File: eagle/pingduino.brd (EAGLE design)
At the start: 98.4 x 80 mm, 35 parts, among them IC1 ATMEGA328, IC3 74LS595N, IC4 74LS595N, IC5 74LS595N, IC6 74LS595N, IC7 74HC14N, Q1 16MHz

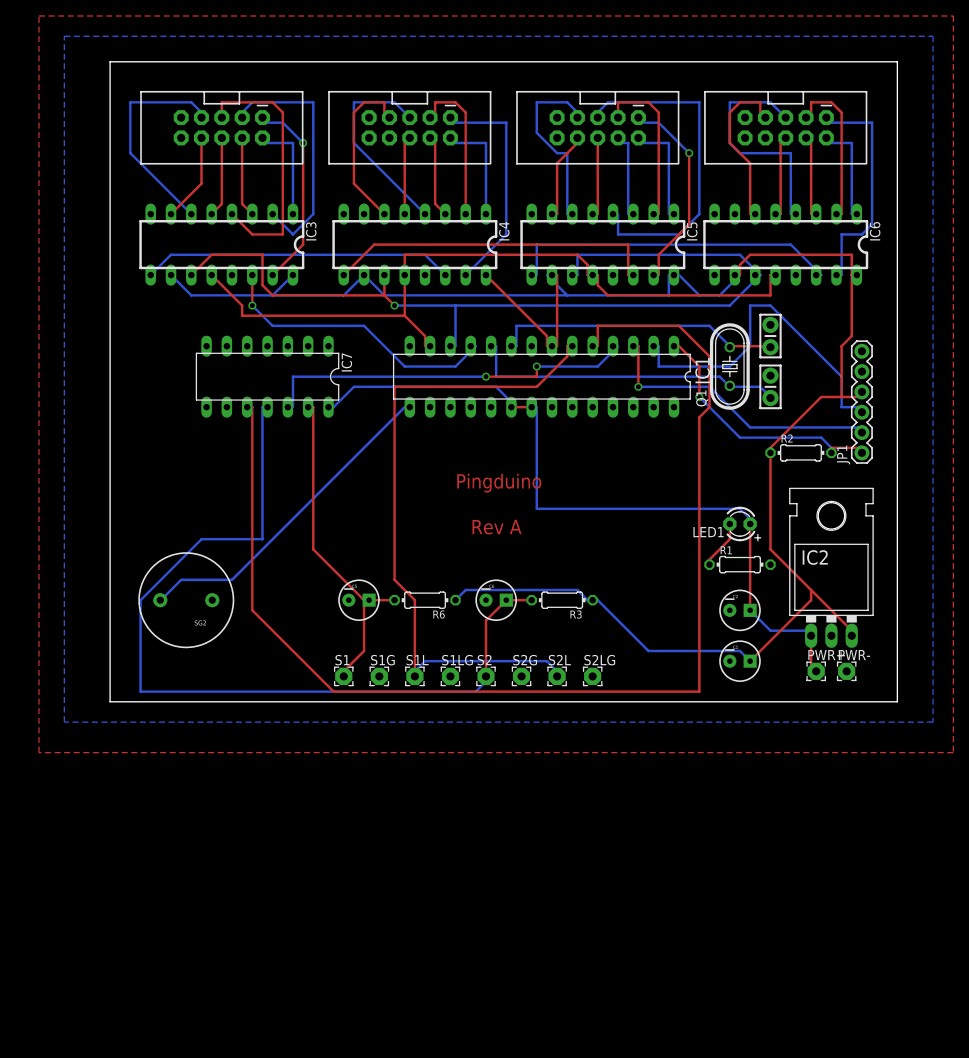
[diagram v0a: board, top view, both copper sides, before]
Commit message: Re-route the 5x2 headers so I can actually solder them.
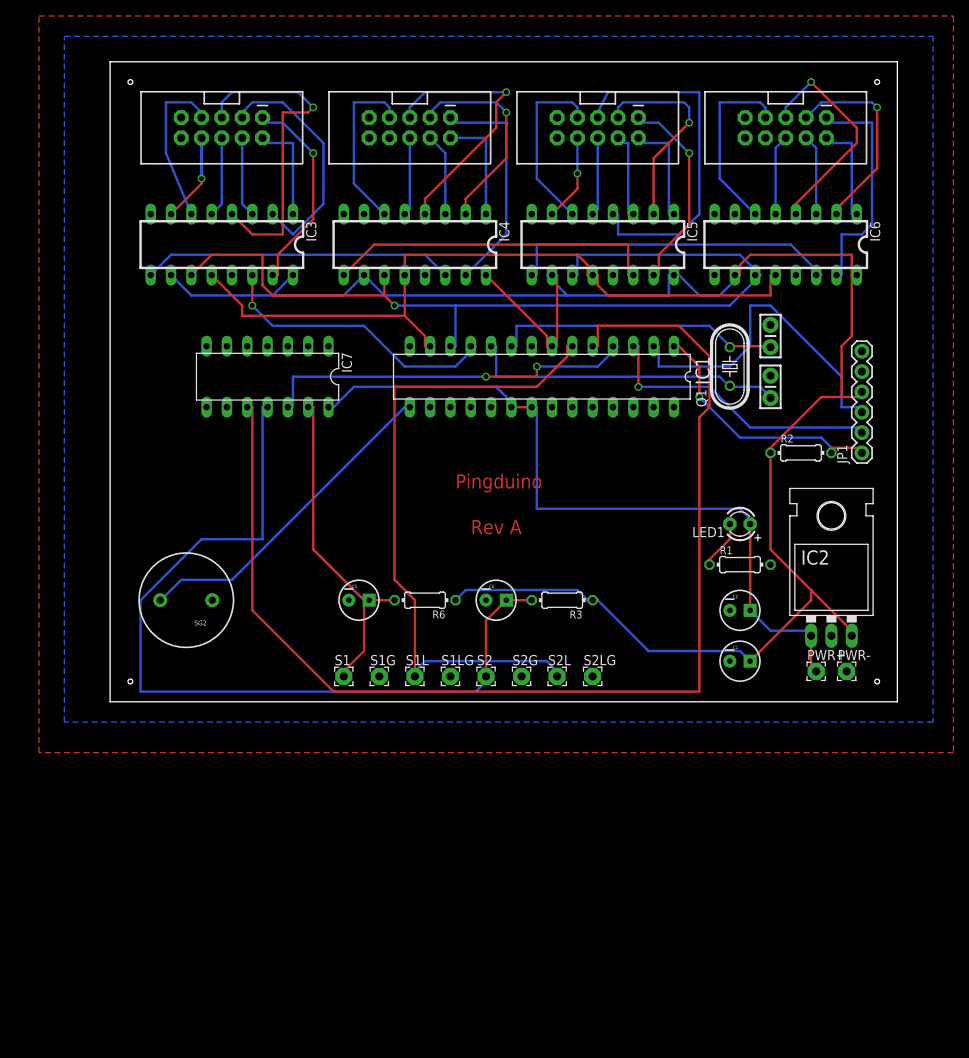
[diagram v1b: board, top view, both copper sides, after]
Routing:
- net D1E: track 32.7 -> 41.4 mm, vias 0 -> 1
- net D2E: track 25.4 -> 33.6 mm
- net D1G: track 27.2 -> 20.2 mm
- net D2C: track 19.2 -> 26.0 mm
- net D4C: track 19.8 -> 25.4 mm
- net D3C: track 20.8 -> 25.9 mm
- net D3E: track 42.2 -> 44.5 mm
- net D4G: track 20.9 -> 23.1 mm
- net D4E: track 29.3 -> 27.8 mm
- net D1A: track 24.9 -> 26.3 mm
- net D1C: track 31.2 -> 30.0 mm
- net D3G: track 23.2 -> 22.4 mm
- net D2G: track 20.8 -> 21.5 mm
- net D1P: vias 0 -> 1

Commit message: Add Garan audio module and amplifier to schematic and board
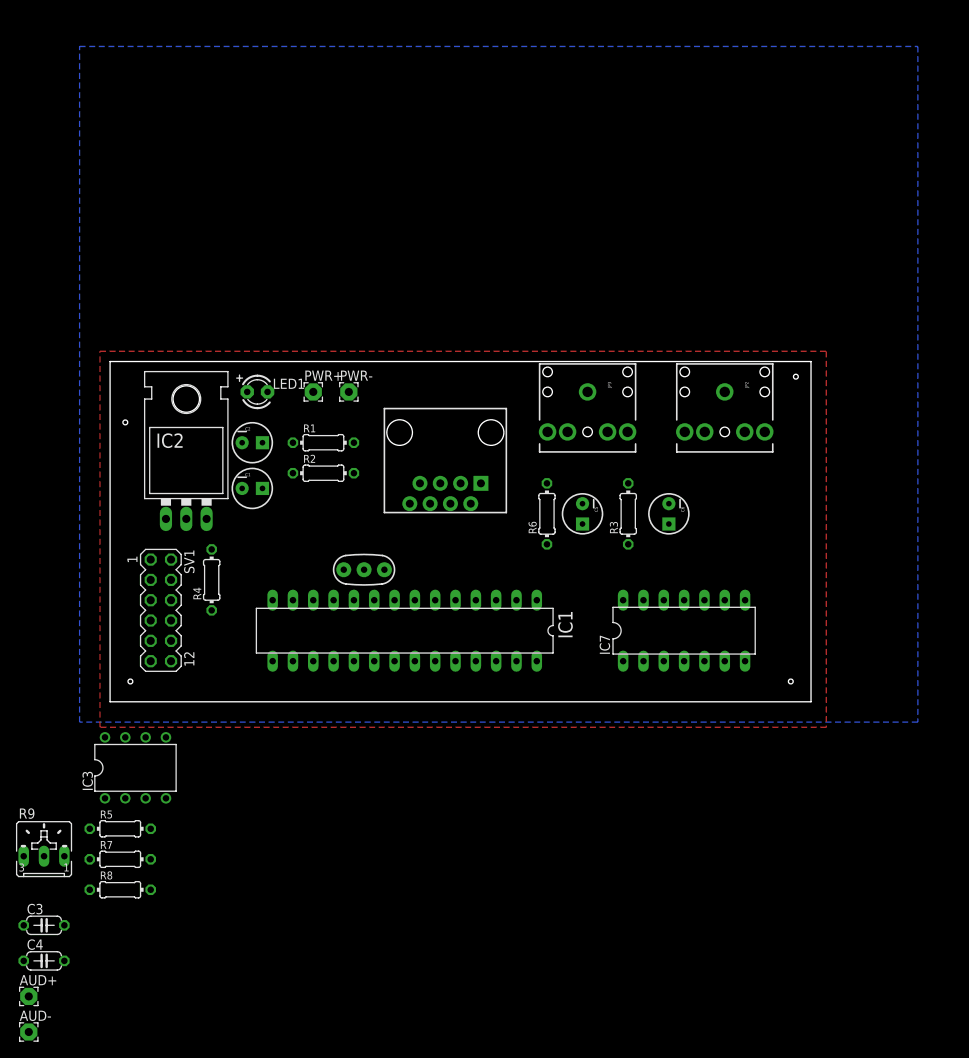
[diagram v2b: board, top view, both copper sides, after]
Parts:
- removed IC4, IC5, IC6: 74LS595N, SparkFun-DigitalIC:DIL16
- removed JP1: (no value), SparkFun-Connectors:1X06
- removed JP4, JP5: (no value), SparkFun-Connectors:2X5-SHROUDED
- removed Q1: 16MHz, adafruit:HC49U-V
- removed S1, S1G, S1L, S1LG, S2, S2G, S2L, S2LG: (no value), wirepad:2,15/1,0
- removed SG2: BUZZER, SparkFun-Electromechanical:BUZZER-12MM
- added AUD+, AUD-: (no value), wirepad:2,15/1,0
- added R4, R5, R7, R8: 1k, resistor:0204/7
- added R9: (no value), pot:B25U
- added SV1: (no value), con-lstb:MA06-2
- added U$1: RJ45-8PTH, SparkFun-Connectors:RJ45-8
- added Y1: (no value), SparkFun-FreqCtrl:RESONATOR-PTH
- C3, C4: value 22p -> (none); device SparkFun-Capacitors:CAP-PTH-SMALL-KIT -> rcl:C050-024X044
- IC3: value 74LS595N -> LM386N-3; device SparkFun-DigitalIC:DIL16 -> linear:DIL08
- JP2, JP3: device SparkFun-Connectors:2X5-SHROUDED -> SparkFun-Connectors:AUDIO-JACK
- moved C4 119.8 mm to (-8.26, -32.4), turned to 0 degrees
- moved C3 113.0 mm to (-8.26, -27.9), turned to 0 degrees
- moved IC2 82.0 mm to (9.53, 26.7)
- moved PWR+ 71.9 mm to (25.4, 38.7)
- moved PWR- 71.4 mm to (29.8, 38.7)
- moved JP2 71.0 mm to (76.8, 38.7)
- moved IC3 66.3 mm to (3.17, -8.26), turned to 0 degrees
- moved C1 64.7 mm to (17.8, 26.7)
- moved C2 64.5 mm to (17.8, 32.4)
- moved LED1 62.5 mm to (18.4, 38.7), turned to 0 degrees
- moved IC7 61.0 mm to (71.8, 8.89), turned to 0 degrees
- moved R2 59.7 mm to (26.7, 28.6)
- moved R1 54.3 mm to (26.7, 32.4)
- moved JP3 39.8 mm to (59.7, 38.7)
- moved IC1 36.1 mm to (36.8, 8.89)
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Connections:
- removed net +5V: C1.1, IC1.7, IC2.OUT, IC3.10, IC3.16, IC4.10, IC4.16, IC5.10, IC5.16, IC6.10, IC6.16, JP1.4, R2.1, R3.1, R6.1
- removed net CLK: IC1.12, IC3.11, IC4.11, IC5.11, IC6.11
- removed net D1A: IC3.15, JP2.1
- removed net D1B: IC3.1, JP2.2
- removed net D1C: IC3.2, JP2.3
- removed net D1D: IC3.3, JP2.4
- removed net D1E: IC3.4, JP2.5
- removed net D1F: IC3.5, JP2.6
- removed net D1G: IC3.6, JP2.7
- removed net D1P: IC3.7, JP2.8
- removed net D2A: IC4.15, JP3.1
- removed net D2B: IC4.1, JP3.2
- removed net D2C: IC4.2, JP3.3
- removed net D2D: IC4.3, JP3.4
- removed net D2E: IC4.4, JP3.5
- removed net D2F: IC4.5, JP3.6
- removed net D2G: IC4.6, JP3.7
- removed net D3A: IC5.15, JP4.1
- removed net D3B: IC5.1, JP4.2
- removed net D3C: IC5.2, JP4.3
- removed net D3D: IC5.3, JP4.4
- removed net D3E: IC5.4, JP4.5
- removed net D3F: IC5.5, JP4.6
- removed net D3G: IC5.6, JP4.7
- removed net D3P: IC5.7, JP4.8
- removed net D4A: IC6.15, JP5.1
- removed net D4B: IC6.1, JP5.2
- removed net D4C: IC6.2, JP5.3
- removed net D4D: IC6.3, JP5.4
- removed net D4E: IC6.4, JP5.5
- removed net D4F: IC6.5, JP5.6
- removed net D4G: IC6.6, JP5.7
- removed net DATA: IC1.11, IC3.14
- removed net LATCH: IC1.13, IC3.12, IC4.12, IC5.12, IC6.12
- removed net N$11: IC4.9, IC5.14
- removed net N$9: IC1.15, SG2.+
- removed net RESET: IC1.1, JP1.1, R2.2
- removed net RXI: IC1.3, JP1.2
- removed net TXO: IC1.2, JP1.3
- new net 12V: C2.1, IC2.IN, LED1.A, PWR+.1, U$1.8
- new net AL: R5.1, SV1.8
- new net AR: R7.1, SV1.6
- new net ARX: IC1.13, IC1.14, R4.2, U$1.7
- new net ATX: IC1.12, SV1.12
- new net N$1: IC1.10, Y1.3
- new net N$14: IC3.3, R9.S
- new net N$16: C3.1, C4.1, IC3.5
- new net N$17: C4.2, R8.2
- new net N$18: AUD+.1, C3.2
- net GND: now also AUD-.1, IC3.2, IC3.4, JP2.SLEEVE, JP3.SLEEVE, R8.1, R9.A, SV1.4, U$1.1, Y1.2; no longer C3.2, C4.2, IC3.13, IC3.8, IC4.13, IC4.8, IC5.13, IC5.8, IC6.13, IC6.8, JP1.5, JP1.6, JP2.10, JP3.10, JP4.10, JP5.10, S1G.1, S1LG.1, S2G.1, S2LG.1, SG2.-
- net N$10: now also R4.1, SV1.11; no longer IC3.9, IC4.14
- net N$12: now also R5.2, R7.2, R9.E; no longer IC5.9, IC6.14
- net N$2: now also Y1.1; no longer C4.1, Q1.2
- net N$4: now also IC1.1, R2.2; no longer C3.1, IC1.10, Q1.1
- net N$6: no longer S2.1
- net N$8: now also JP2.RING; no longer S1.1
- net SLED: now also JP2.TIP, JP3.TIP; no longer S1L.1, S2L.1
- net VCC: now also C1.1, IC1.7, IC2.OUT, IC3.6, R2.1, R3.1, R6.1, SV1.1; no longer C2.1, IC2.IN, LED1.A, PWR+.1
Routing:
- net +5V: track 241.0 -> 0.00 mm
- net N$7: track 147.3 -> 0.00 mm
- net CLK: track 114.6 -> 0.00 mm, vias 1 -> 0
- net N$6: track 105.1 -> 0.00 mm
- net VCC: track 95.1 -> 0.00 mm
- net LATCH: track 92.6 -> 0.00 mm
- net SLED: track 82.4 -> 0.00 mm
- net N$5: track 48.0 -> 0.00 mm, vias 2 -> 0
- net D3E: track 44.5 -> 0.00 mm
- net TXO: track 42.8 -> 0.00 mm
- net N$12: track 42.2 -> 0.00 mm
- net N$8: track 41.8 -> 0.00 mm
- net N$11: track 41.6 -> 0.00 mm
- net D1E: track 41.4 -> 0.00 mm, vias 1 -> 0
- net N$9: track 41.2 -> 0.00 mm
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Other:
- board size 98.4 x 80 mm -> 87.6 x 42.5 mm
- board text removed: "Pingduino"
- board text removed: "Rev A"
